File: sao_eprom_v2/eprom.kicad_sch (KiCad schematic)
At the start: 7 parts

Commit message: the experiment
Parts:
- removed U? (x2): 74HC273, Package_SO:TSSOP-20_4.4x6.5mm_P0.65mm, symbol 74xx:74HC273
- added U4, U7: 74LS573, Package_SO:TSSOP-20_4.4x6.5mm_P0.65mm, symbol 74xx:74LS573
- renumbered D2 to D1, D3 to D2, D1 to D3
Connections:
- net +3V3: now also U4.20 (VCC), U7.20 (VCC)
- net A0: now also U4.2 (D0), U7.2 (D0)
- net A1: now also U4.3 (D1), U7.3 (D1)
- net A2: now also U4.4 (D2), U7.4 (D2)
- net A3: now also U4.5 (D3), U7.5 (D3)
- net A4: now also U4.6 (D4), U7.6 (D4)
- net A5: now also U4.7 (D5), U7.7 (D5)
- net A6: now also U4.8 (D6), U7.8 (D6)
- net A7: now also U4.9 (D7), U7.9 (D7)
- net AHS: now also U7.11 (Load)
- net ALS: now also U4.11 (Load)
- net GND: now also U4.1 (OE), U4.10 (GND), U7.1 (OE), U7.10 (GND)
- net at D3.2 (A): now also U7.18 (Q1)
- net at D1.2 (A): now also U7.12 (Q7)
- net D7H: now reaches U?.10 (A7), U?.19 (D7)
- net D0H: now reaches U?.11 (D0), U?.3 (A0)
- net D1H: now reaches U?.12 (D1), U?.4 (A1)
- net D2H: now reaches U?.13 (D2), U?.5 (A2)
- net D3H: now reaches U?.15 (D3), U?.6 (A3)
- net D4H: now reaches U?.16 (D4), U?.7 (A4)
- net D5H: now reaches U?.17 (D5), U?.8 (A5)
- net D6H: now reaches U?.18 (D6), U?.9 (A6)
- net Q4: now reaches U?.6 (A4)
- net Q4: now also U4.15 (Q4)
- net Q5: now reaches U?.5 (A5)
- net Q5: now also U4.14 (Q5)
- net Q6: now reaches U?.4 (A6)
- net Q6: now also U4.13 (Q6)
- net Q7: now reaches U?.3 (A7)
- net Q7: now also U4.12 (Q7)
- net Q0: now reaches U?.10 (A0)
- net Q0: now also U4.19 (Q0)
- net Q1: now reaches U?.9 (A1)
- net Q1: now also U4.18 (Q1)
- net Q2: now reaches U?.8 (A2)
- net Q2: now also U4.17 (Q2)
- net Q3: now reaches U?.7 (A3)
- net Q3: now also U4.16 (Q3)
- net Q12: now reaches U?.2 (A12)
- net Q12: now also U7.15 (Q4)
- net Q13: now reaches U?.26 (A13)
- net Q13: now also U7.14 (Q5)
- net Q14: now reaches U?.27 (A14)
- net Q14: now also U7.13 (Q6)
- net Q8: now reaches U?.25 (A8)
- net Q8: now also U7.19 (Q0)
- net Q10: now reaches U?.21 (A10)
- net Q10: now also U7.17 (Q2)
- net Q11: now reaches U?.23 (A11)
- net Q11: now also U7.16 (Q3)

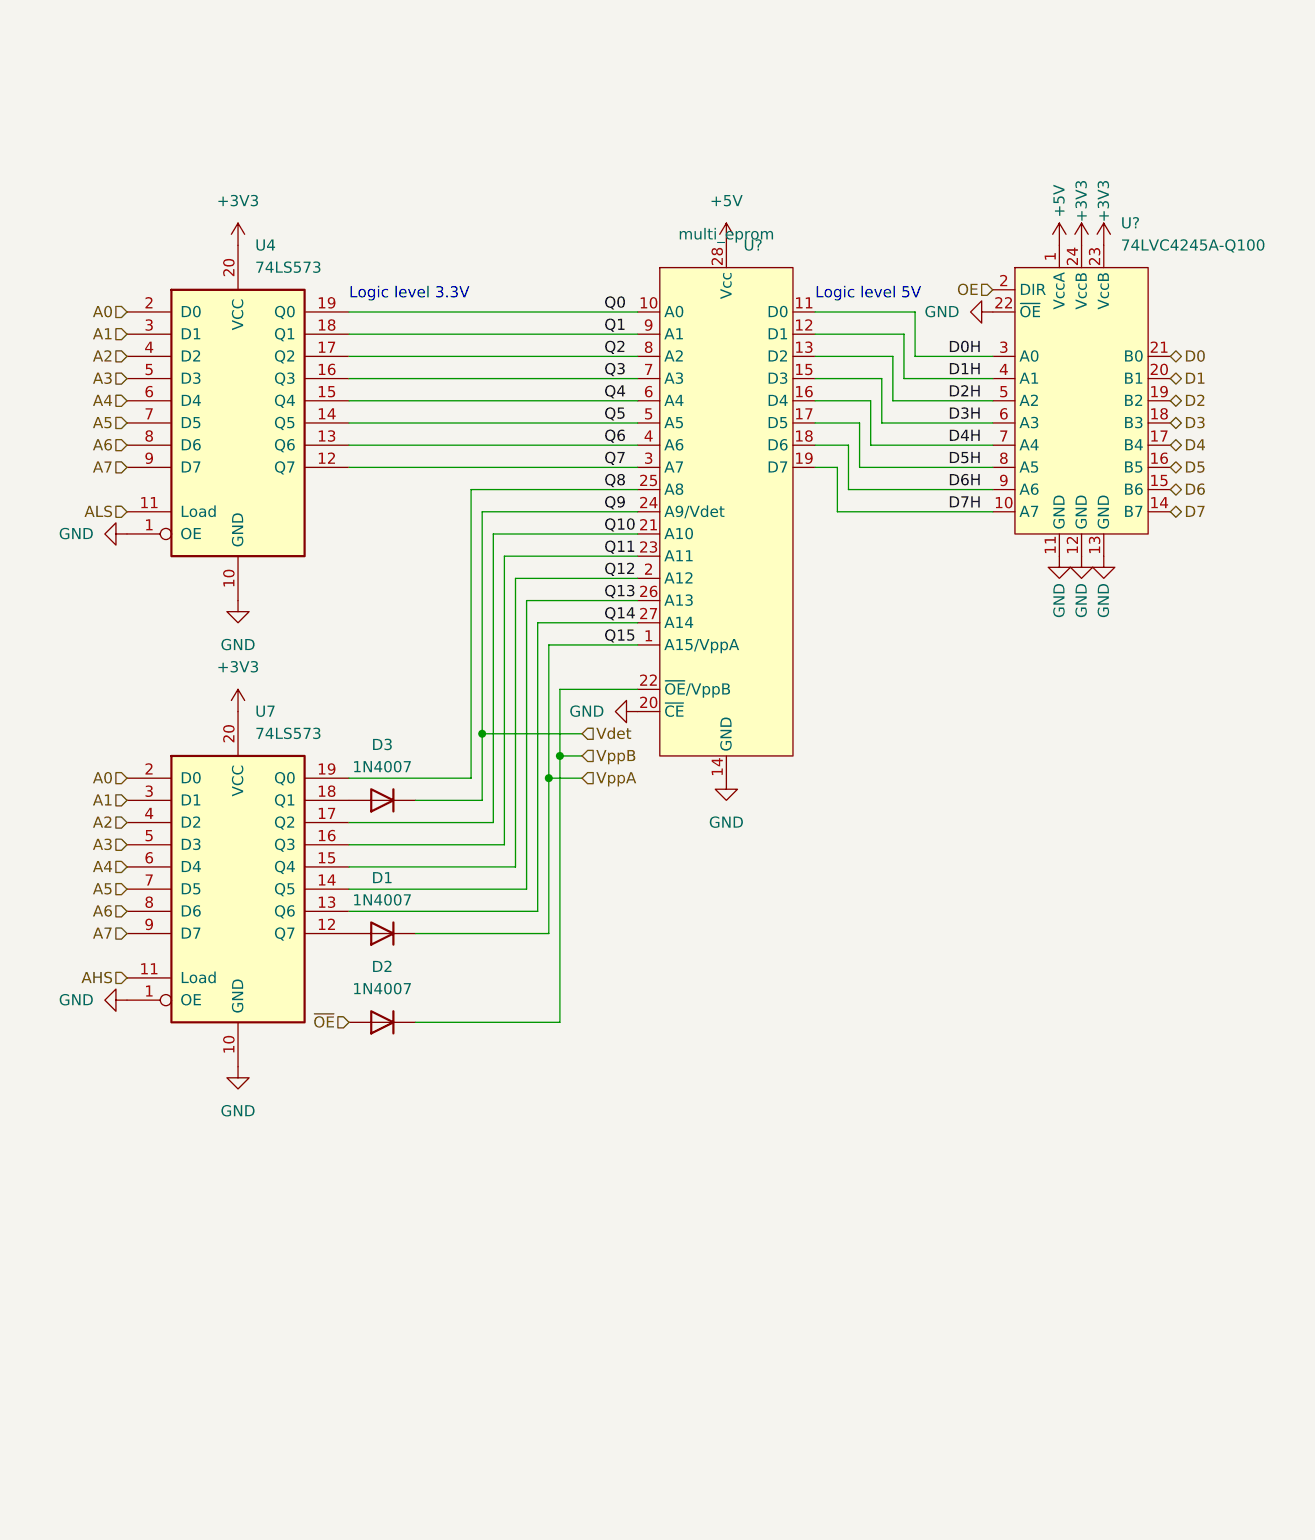
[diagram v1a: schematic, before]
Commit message: Flip the CHIPS upside down to make routing easier
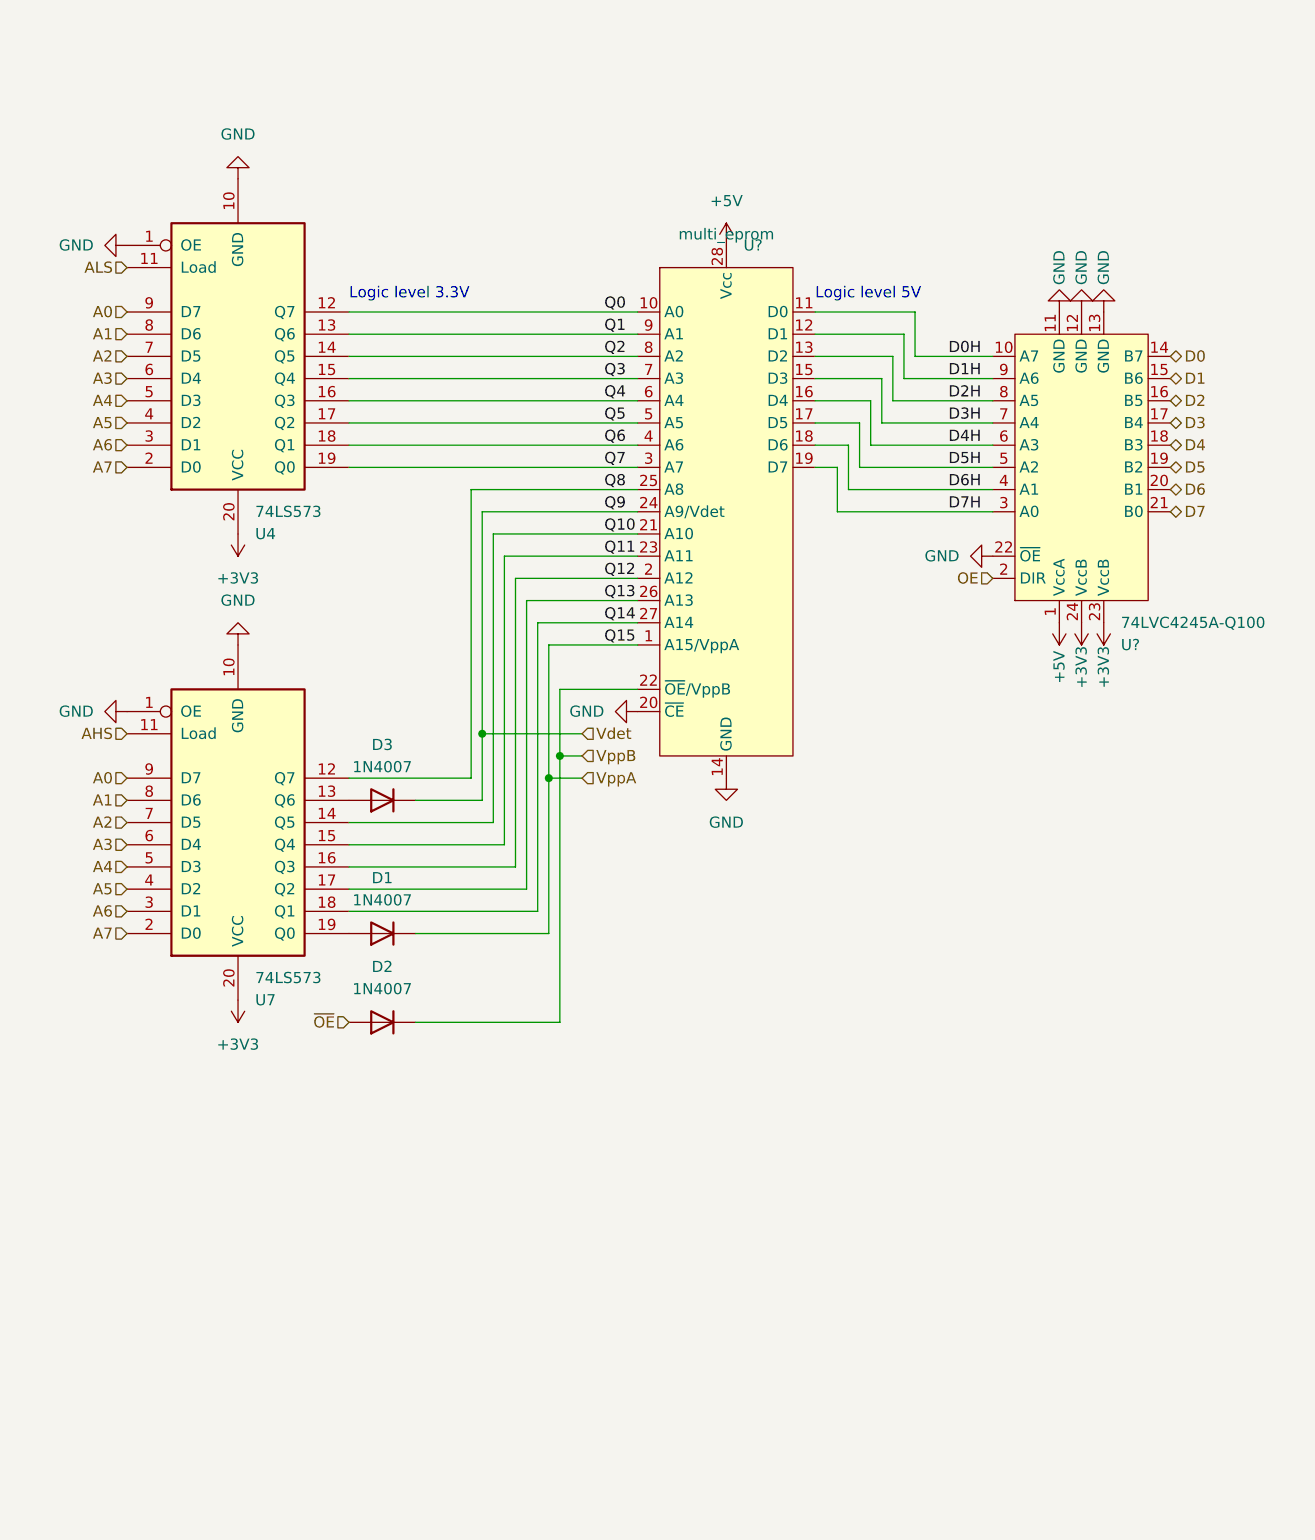
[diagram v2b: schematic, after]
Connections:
- net A0: now also U4.9 (D7), U7.9 (D7); no longer U4.2 (D0), U7.2 (D0)
- net A1: now also U4.8 (D6), U7.8 (D6); no longer U4.3 (D1), U7.3 (D1)
- net A2: now also U4.7 (D5), U7.7 (D5); no longer U4.4 (D2), U7.4 (D2)
- net A3: now also U4.6 (D4), U7.6 (D4); no longer U4.5 (D3), U7.5 (D3)
- net A4: now also U4.5 (D3), U7.5 (D3); no longer U4.6 (D4), U7.6 (D4)
- net A5: now also U4.4 (D2), U7.4 (D2); no longer U4.7 (D5), U7.7 (D5)
- net A6: now also U4.3 (D1), U7.3 (D1); no longer U4.8 (D6), U7.8 (D6)
- net A7: now also U4.2 (D0), U7.2 (D0); no longer U4.9 (D7), U7.9 (D7)
- net D0: now also U?.14 (B7); no longer U?.21 (B0)
- net D0H: now also U?.10 (A7); no longer U?.3 (A0)
- net D1: now also U?.15 (B6); no longer U?.20 (B1)
- net D1H: now also U?.9 (A6); no longer U?.4 (A1)
- net D2: now also U?.16 (B5); no longer U?.19 (B2)
- net D2H: now also U?.8 (A5); no longer U?.5 (A2)
- net D3: now also U?.17 (B4); no longer U?.18 (B3)
- net D3H: now also U?.7 (A4); no longer U?.6 (A3)
- net D4: now also U?.18 (B3); no longer U?.17 (B4)
- net D4H: now also U?.6 (A3); no longer U?.7 (A4)
- net D5: now also U?.19 (B2); no longer U?.16 (B5)
- net D5H: now also U?.5 (A2); no longer U?.8 (A5)
- net D6: now also U?.20 (B1); no longer U?.15 (B6)
- net D6H: now also U?.4 (A1); no longer U?.9 (A6)
- net D7: now also U?.21 (B0); no longer U?.14 (B7)
- net D7H: now also U?.3 (A0); no longer U?.10 (A7)
- net Q0: now also U4.12 (Q7); no longer U4.19 (Q0)
- net Q1: now also U4.13 (Q6); no longer U4.18 (Q1)
- net Q10: now also U7.14 (Q5); no longer U7.17 (Q2)
- net Q11: now also U7.15 (Q4); no longer U7.16 (Q3)
- net Q12: now also U7.16 (Q3); no longer U7.15 (Q4)
- net Q13: now also U7.17 (Q2); no longer U7.14 (Q5)
- net Q14: now also U7.18 (Q1); no longer U7.13 (Q6)
- net Q2: now also U4.14 (Q5); no longer U4.17 (Q2)
- net Q3: now also U4.15 (Q4); no longer U4.16 (Q3)
- net Q4: now also U4.16 (Q3); no longer U4.15 (Q4)
- net Q5: now also U4.17 (Q2); no longer U4.14 (Q5)
- net Q6: now also U4.18 (Q1); no longer U4.13 (Q6)
- net Q7: now also U4.19 (Q0); no longer U4.12 (Q7)
- net Q8: now also U7.12 (Q7); no longer U7.19 (Q0)
- net at D3.2 (A): now also U7.13 (Q6); no longer U7.18 (Q1)
- net at D1.2 (A): now also U7.19 (Q0); no longer U7.12 (Q7)
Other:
- moved on the sheet: U4, U7, U?

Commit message: More tricky routing.
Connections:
- net D0: now also U?.21 (B0); no longer U?.14 (B7)
- net D0H: now also U?.3 (A0); no longer U?.10 (A7)
- net D1: now also U?.20 (B1); no longer U?.15 (B6)
- net D1H: now also U?.4 (A1); no longer U?.9 (A6)
- net D2: now also U?.19 (B2); no longer U?.16 (B5)
- net D2H: now also U?.5 (A2); no longer U?.8 (A5)
- net D3: now also U?.18 (B3); no longer U?.17 (B4)
- net D3H: now also U?.6 (A3); no longer U?.7 (A4)
- net D4: now also U?.17 (B4); no longer U?.18 (B3)
- net D4H: now also U?.7 (A4); no longer U?.6 (A3)
- net D5: now also U?.16 (B5); no longer U?.19 (B2)
- net D5H: now also U?.8 (A5); no longer U?.5 (A2)
- net D6: now also U?.15 (B6); no longer U?.20 (B1)
- net D6H: now also U?.9 (A6); no longer U?.4 (A1)
- net D7: now also U?.14 (B7); no longer U?.21 (B0)
- net D7H: now also U?.10 (A7); no longer U?.3 (A0)
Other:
- moved on the sheet: U?
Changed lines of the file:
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@@
     (effects (font (size 1.27 1.27)) (justify left))
   )
-  (hierarchical_label "OE" (shape input) (at 157.48 76.2 180) (fields_autoplaced)
+  (hierarchical_label "OE" (shape input) (at 157.48 43.18 180) (fields_autoplaced)
     (effects (font (size 1.27 1.27)) (justify right))
   )
@@
     (effects (font (size 1.27 1.27)) (justify left))
   )
-  (symbol (lib_id "power:GND") (at 165.1 45.72 0) (mirror x) (unit 1)
+  (symbol (lib_id "power:GND") (at 165.1 73.66 0) (unit 1)
     (in_bom yes) (on_board yes) (dnp no)
-    (property "Reference" "#PWR?" (at 165.1 39.37 0)
-      (effects (font (size 1.27 1.27)) hide)
-    )
-    (property "Value" "GND" (at 165.1 40.64 90)
-      (effects (font (size 1.27 1.27)))
-    )
-    (property "Footprint" "" (at 165.1 45.72 0)
-      (effects (font (size 1.27 1.27)) hide)
-    )
-    (property "Datasheet" "" (at 165.1 45.72 0)
+    (property "Reference" "#PWR?" (at 165.1 80.01 0)
+      (effects (font (size 1.27 1.27)) hide)
+    )
+    (property "Value" "GND" (at 165.1 78.74 90)
+      (effects (font (size 1.27 1.27)))
+    )
+    (property "Footprint" "" (at 165.1 73.66 0)
+      (effects (font (size 1.27 1.27)) hide)
+    )
+    (property "Datasheet" "" (at 165.1 73.66 0)
       (effects (font (size 1.27 1.27)) hide)
     )
@@
     )
   )
-  (symbol (lib_id "power:GND") (at 167.64 45.72 0) (mirror x) (unit 1)
+  (symbol (lib_id "power:GND") (at 167.64 73.66 0) (unit 1)
     (in_bom yes) (on_board yes) (dnp no)
-    (property "Reference" "#PWR?" (at 167.64 39.37 0)
-      (effects (font (size 1.27 1.27)) hide)
-    )
-    (property "Value" "GND" (at 167.64 40.64 90)
-      (effects (font (size 1.27 1.27)))
-    )
-    (property "Footprint" "" (at 167.64 45.72 0)
-      (effects (font (size 1.27 1.27)) hide)
-    )
-    (property "Datasheet" "" (at 167.64 45.72 0)
+    (property "Reference" "#PWR?" (at 167.64 80.01 0)
+      (effects (font (size 1.27 1.27)) hide)
+    )
+    (property "Value" "GND" (at 167.64 78.74 90)
+      (effects (font (size 1.27 1.27)))
+    )
+    (property "Footprint" "" (at 167.64 73.66 0)
+      (effects (font (size 1.27 1.27)) hide)
+    )
+    (property "Datasheet" "" (at 167.64 73.66 0)
       (effects (font (size 1.27 1.27)) hide)
     )
@@
     )
   )
-  (symbol (lib_id "power:GND") (at 157.48 73.66 270) (mirror x) (unit 1)
-    (in_bom yes) (on_board yes) (dnp no) (fields_autoplaced)
-    (property "Reference" "#PWR?" (at 151.13 73.66 0)
-      (effects (font (size 1.27 1.27)) hide)
-    )
-    (property "Value" "GND" (at 153.67 73.66 90)
+  (symbol (lib_id "power:GND") (at 157.48 45.72 270) (unit 1)
+    (in_bom yes) (on_board yes) (dnp no) (fields_autoplaced)
+    (property "Reference" "#PWR?" (at 151.13 45.72 0)
+      (effects (font (size 1.27 1.27)) hide)
+    )
+    (property "Value" "GND" (at 153.67 45.72 90)
       (effects (font (size 1.27 1.27)) (justify right))
     )
-    (property "Footprint" "" (at 157.48 73.66 0)
-      (effects (font (size 1.27 1.27)) hide)
-    )
-    (property "Datasheet" "" (at 157.48 73.66 0)
+    (property "Footprint" "" (at 157.48 45.72 0)
+      (effects (font (size 1.27 1.27)) hide)
+    )
+    (property "Datasheet" "" (at 157.48 45.72 0)
       (effects (font (size 1.27 1.27)) hide)
     )
@@
     )
   )
-  (symbol (lib_id "74lvc4245a-q100:74LVC4245A-Q100") (at 167.64 62.23 0) (mirror x) (unit 1)
-    (in_bom yes) (on_board yes) (dnp no) (fields_autoplaced)
-    (property "Reference" "U?" (at 172.1359 83.82 0)
+  (symbol (lib_id "74lvc4245a-q100:74LVC4245A-Q100") (at 167.64 57.15 0) (unit 1)
+    (in_bom yes) (on_board yes) (dnp no) (fields_autoplaced)
+    (property "Reference" "U?" (at 172.1359 35.56 0)
       (effects (font (size 1.27 1.27)) (justify left))
     )
-    (property "Value" "74LVC4245A-Q100" (at 172.1359 81.28 0)
+    (property "Value" "74LVC4245A-Q100" (at 172.1359 38.1 0)
       (effects (font (size 1.27 1.27)) (justify left))
     )
-    (property "Footprint" "Package_SO:TSSOP-24_4.4x7.8mm_P0.65mm" (at 167.64 92.71 0)
-      (effects (font (size 1.27 1.27)) hide)
-    )
-    (property "Datasheet" "https://datasheet.lcsc.com/lcsc/2007030233_Nexperia-74LVC4245APW-Q100J_C548801.pdf" (at 167.64 92.71 0)
+    (property "Footprint" "Package_SO:TSSOP-24_4.4x7.8mm_P0.65mm" (at 167.64 26.67 0)
+      (effects (font (size 1.27 1.27)) hide)
+    )
+    (property "Datasheet" "https://datasheet.lcsc.com/lcsc/2007030233_Nexperia-74LVC4245APW-Q100J_C548801.pdf" (at 167.64 26.67 0)
       (effects (font (size 1.27 1.27)) hide)
     )
@@
     )
   )
-  (symbol (lib_id "power:+3V3") (at 170.18 81.28 0) (mirror x) (unit 1)
+  (symbol (lib_id "power:+3V3") (at 170.18 38.1 0) (unit 1)
     (in_bom yes) (on_board yes) (dnp no)
-    (property "Reference" "#PWR?" (at 170.18 77.47 0)
-      (effects (font (size 1.27 1.27)) hide)
-    )
-    (property "Value" "+3V3" (at 170.18 86.36 90)
-      (effects (font (size 1.27 1.27)))
-    )
-    (property "Footprint" "" (at 170.18 81.28 0)
-      (effects (font (size 1.27 1.27)) hide)
-    )
-    (property "Datasheet" "" (at 170.18 81.28 0)
+    (property "Reference" "#PWR?" (at 170.18 41.91 0)
+      (effects (font (size 1.27 1.27)) hide)
+    )
+    (property "Value" "+3V3" (at 170.18 33.02 90)
+      (effects (font (size 1.27 1.27)))
+    )
+    (property "Footprint" "" (at 170.18 38.1 0)
+      (effects (font (size 1.27 1.27)) hide)
+    )
+    (property "Datasheet" "" (at 170.18 38.1 0)
       (effects (font (size 1.27 1.27)) hide)
     )
@@
     )
   )
-  (symbol (lib_id "power:GND") (at 170.18 45.72 0) (mirror x) (unit 1)
+  (symbol (lib_id "power:GND") (at 170.18 73.66 0) (unit 1)
     (in_bom yes) (on_board yes) (dnp no)
-    (property "Reference" "#PWR?" (at 170.18 39.37 0)
-      (effects (font (size 1.27 1.27)) hide)
-    )
-    (property "Value" "GND" (at 170.18 40.64 90)
-      (effects (font (size 1.27 1.27)))
-    )
-    (property "Footprint" "" (at 170.18 45.72 0)
-      (effects (font (size 1.27 1.27)) hide)
-    )
-    (property "Datasheet" "" (at 170.18 45.72 0)
+    (property "Reference" "#PWR?" (at 170.18 80.01 0)
+      (effects (font (size 1.27 1.27)) hide)
+    )
+    (property "Value" "GND" (at 170.18 78.74 90)
+      (effects (font (size 1.27 1.27)))
+    )
+    (property "Footprint" "" (at 170.18 73.66 0)
+      (effects (font (size 1.27 1.27)) hide)
+    )
+    (property "Datasheet" "" (at 170.18 73.66 0)
       (effects (font (size 1.27 1.27)) hide)
     )
@@
     )
   )
-  (symbol (lib_id "power:+3V3") (at 167.64 81.28 0) (mirror x) (unit 1)
+  (symbol (lib_id "power:+3V3") (at 167.64 38.1 0) (unit 1)
     (in_bom yes) (on_board yes) (dnp no)
-    (property "Reference" "#PWR?" (at 167.64 77.47 0)
-      (effects (font (size 1.27 1.27)) hide)
-    )
-    (property "Value" "+3V3" (at 167.64 86.36 90)
-      (effects (font (size 1.27 1.27)))
-    )
-    (property "Footprint" "" (at 167.64 81.28 0)
-      (effects (font (size 1.27 1.27)) hide)
-    )
-    (property "Datasheet" "" (at 167.64 81.28 0)
+    (property "Reference" "#PWR?" (at 167.64 41.91 0)
+      (effects (font (size 1.27 1.27)) hide)
+    )
+    (property "Value" "+3V3" (at 167.64 33.02 90)
+      (effects (font (size 1.27 1.27)))
+    )
+    (property "Footprint" "" (at 167.64 38.1 0)
+      (effects (font (size 1.27 1.27)) hide)
+    )
+    (property "Datasheet" "" (at 167.64 38.1 0)
       (effects (font (size 1.27 1.27)) hide)
     )
@@
     )
   )
-  (symbol (lib_id "power:+5V") (at 165.1 81.28 0) (mirror x) (unit 1)
+  (symbol (lib_id "power:+5V") (at 165.1 38.1 0) (unit 1)
     (in_bom yes) (on_board yes) (dnp no)
-    (property "Reference" "#PWR?" (at 165.1 77.47 0)
-      (effects (font (size 1.27 1.27)) hide)
-    )
-    (property "Value" "+5V" (at 165.1 86.36 90)
-      (effects (font (size 1.27 1.27)))
-    )
-    (property "Footprint" "" (at 165.1 81.28 0)
-      (effects (font (size 1.27 1.27)) hide)
-    )
-    (property "Datasheet" "" (at 165.1 81.28 0)
-      (effects (font (size 1.27 1.27)) hide)
-    )
+    (property "Reference" "#PWR?" (at 165.1 41.91 0)
+      (effects (font (size 1.27 1.27)) hide)
+    )
+    (property "Value" "+5V" (at 165.1 33.02 90)
+      (effects (font (size 1.27 1.27)))
+    )
+    (property "Footprint" "" (at 165.1 38.1 0)
+      (effects (font (size 1.27 1.27)) hide)
+    )
+    (property "Datasheet" "" (at 165.1 38.1 0)
+      (effects (font (size 1.27 1.27)) hide)
+    )

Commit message: Nearly finished the design
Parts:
- renumbered D2 to D1, D1 to D2
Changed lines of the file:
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@@
   (symbol (lib_id "Diode:1N4007") (at 87.63 127 180) (unit 1)
     (in_bom yes) (on_board yes) (dnp no) (fields_autoplaced)
-    (property "Reference" "D2" (at 87.63 120.65 0)
+    (property "Reference" "D1" (at 87.63 120.65 0)
       (effects (font (size 1.27 1.27)))
     )
@@
       (project "sao_eprom_v2"
         (path "/07beccdd-32b3-4f03-aa51-fb5544b6f2d4/1053addf-4f12-44cd-9743-7d35ca2d08ac"
-          (reference "D2") (unit 1)
+          (reference "D1") (unit 1)
         )
       )
@@
   (symbol (lib_id "Diode:1N4007") (at 87.63 116.84 180) (unit 1)
     (in_bom yes) (on_board yes) (dnp no) (fields_autoplaced)
-    (property "Reference" "D1" (at 87.63 110.49 0)
+    (property "Reference" "D2" (at 87.63 110.49 0)
       (effects (font (size 1.27 1.27)))
     )
@@
       (project "sao_eprom_v2"
         (path "/07beccdd-32b3-4f03-aa51-fb5544b6f2d4/1053addf-4f12-44cd-9743-7d35ca2d08ac"
-          (reference "D1") (unit 1)
+          (reference "D2") (unit 1)
         )
       )
